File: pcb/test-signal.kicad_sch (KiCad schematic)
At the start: 9 parts, among them J3 Conn_Coaxial, U13 SN74LVC1G3157DCKR, U150 MCP4821

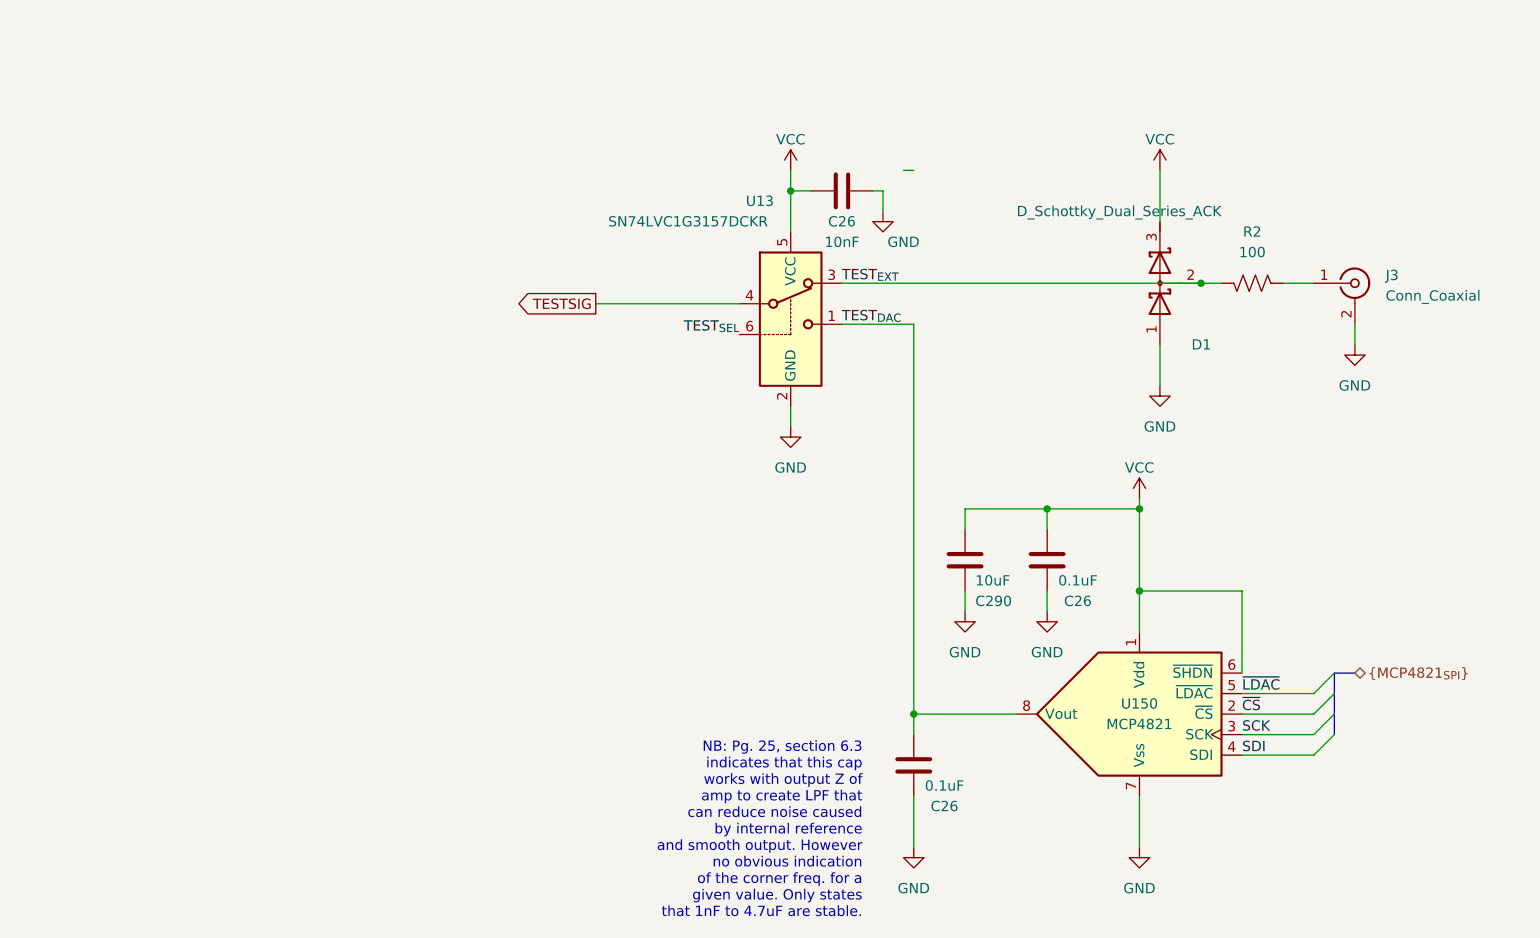
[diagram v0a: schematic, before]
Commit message: Remove battery power option
- This device needs user IO
- Battery power means there would need to be a touch screen or wireless
  connection. Too complex.
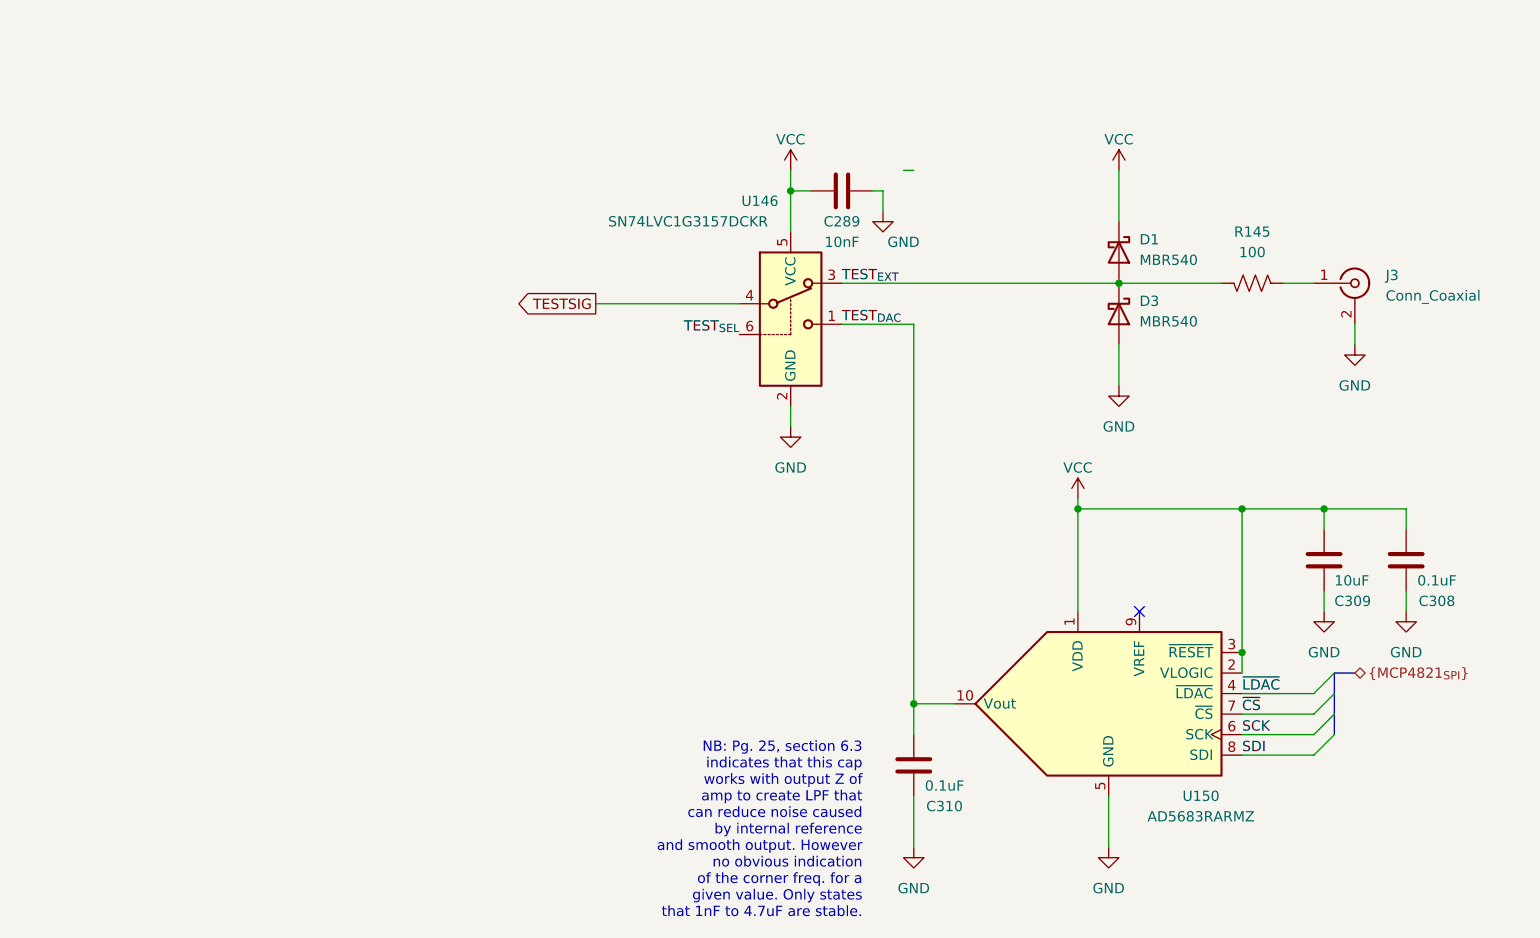
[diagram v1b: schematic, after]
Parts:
- removed D1: D_Schottky_Dual_Series_ACK, symbol Device:D_Schottky_Dual_Series_ACK
- removed U150: MCP4821, symbol Analog_DAC:MCP4821
- added D1, D3: MBR540, Diode_SMD:D_SOD-123, symbol Device:D_Schottky
- added U150: AD5683RARMZ, Package_SO:MSOP-10_3x3mm_P0.5mm, symbol open-ephys:AD568xR
- R145: renamed from R2; footprint Resistor_SMD:R_0805_2012Metric -> Resistor_SMD:R_0402_1005Metric
- renumbered C26 to C289, C26 to C308, C290 to C309, C26 to C310, U13 to U146
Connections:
- net GND: now also D3.2 (A), U150.5 (GND)
- net SCK: now also U150.6 (SCK)
- net SDI: now also U150.8 (SDI)
- net TEST_{DAC}: now also U150.10 (Vout)
- net TEST_{EXT}: now also D1.2 (A), D3.1 (K)
- net VCC: now also D1.1 (K), U150.1 (VDD), U150.2 (VLOGIC), U150.3 (~{RESET})
- net ~{CS}: now also U150.7 (~{CS})
- net ~{LDAC}: now also U150.4 (~{LDAC})
- no-connect marks 0 -> 1
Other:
- moved on the sheet: C308, C309

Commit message: Finished schematic, started routing
- There is a 8-channel motif that will need to be copied 16x on the
  board. I'm not sure the most efficient way to do this.
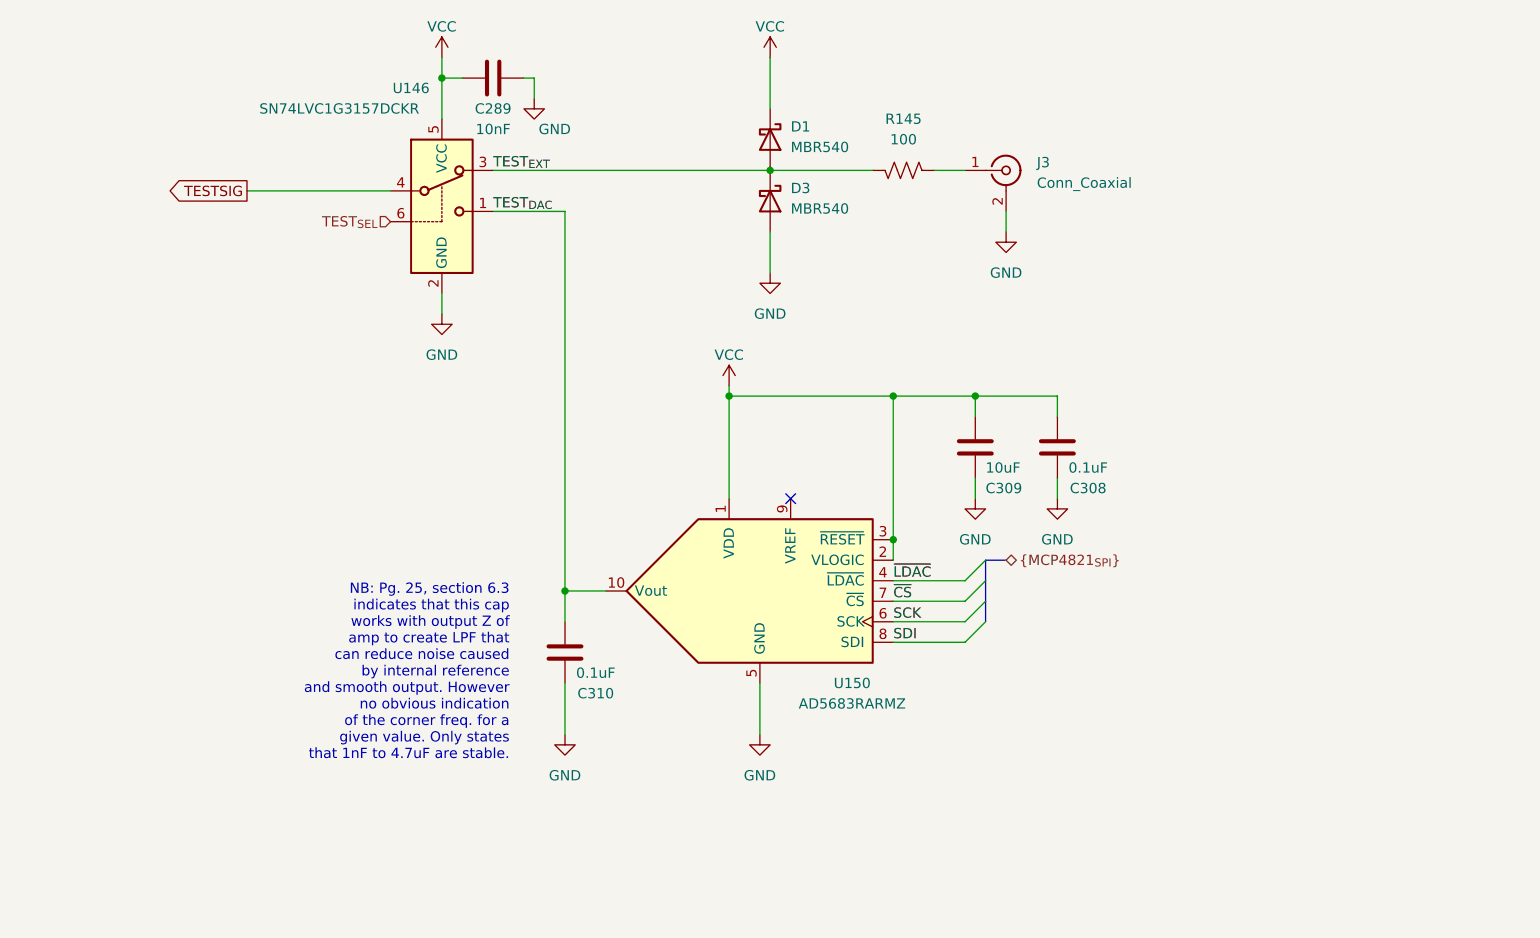
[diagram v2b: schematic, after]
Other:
- moved on the sheet: C289, C308, C309, C310, D1, D3, J3, R145, U146, U150

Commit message: Motif is repeated
- some components are grouped by function
- components are roughly organized within groups
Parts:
- renumbered C289 to C288, C310 to C289, C309 to C290, C308 to C291, D3 to D2, J3 to J5, R145 to R262, U146 to U147, U150 to U148
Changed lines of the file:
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@@
 		(dnp no)
 		(fields_autoplaced yes)
-		(property "Reference" "#PWR0604"
+		(property "Reference" "#PWR0723"
 			(at 127 132.08 0)
 			(effects
@@
 			(project "ephys-test-board"
 				(path "/ffaa6ffd-73fa-4da3-9ff1-78fa7369281f/a1b553e6-360f-440c-99f8-5680e9dd5803"
-					(reference "#PWR0604")
+					(reference "#PWR0723")
 					(unit 1)
 				)
@@
 		(on_board yes)
 		(dnp no)
-		(property "Reference" "C308"
+		(property "Reference" "C291"
 			(at 191.77 95.25 0)
 			(effects
@@
 			(project "ephys-test-board"
 				(path "/ffaa6ffd-73fa-4da3-9ff1-78fa7369281f/a1b553e6-360f-440c-99f8-5680e9dd5803"
-					(reference "C308")
+					(reference "C291")
 					(unit 1)
 				)
@@
 		(on_board yes)
 		(dnp no)
-		(property "Reference" "R145"
+		(property "Reference" "R262"
 			(at 168.91 49.53 90)
 			(effects
@@
 			(project "ephys-test-board"
 				(path "/ffaa6ffd-73fa-4da3-9ff1-78fa7369281f/a1b553e6-360f-440c-99f8-5680e9dd5803"
-					(reference "R145")
+					(reference "R262")
 					(unit 1)
 				)
@@
 		(dnp no)
 		(fields_autoplaced yes)
-		(property "Reference" "#PWR0566"
+		(property "Reference" "#PWR0729"
 			(at 181.61 69.85 0)
 			(effects
@@
 			(project "ephys-test-board"
 				(path "/ffaa6ffd-73fa-4da3-9ff1-78fa7369281f/a1b553e6-360f-440c-99f8-5680e9dd5803"
-					(reference "#PWR0566")
+					(reference "#PWR0729")
 					(unit 1)
 				)
@@
 		(on_board yes)
 		(dnp no)
-		(property "Reference" "#PWR0564"
+		(property "Reference" "#PWR0726"
 			(at 152.4 45.72 0)
 			(effects
@@
 			(project "ephys-test-board"
 				(path "/ffaa6ffd-73fa-4da3-9ff1-78fa7369281f/a1b553e6-360f-440c-99f8-5680e9dd5803"
-					(reference "#PWR0564")
+					(reference "#PWR0726")
 					(unit 1)
 				)
@@
 		(on_board yes)
 		(dnp no)
-		(property "Reference" "U150"
+		(property "Reference" "U148"
 			(at 162.56 119.38 0)
 			(effects
@@
 			(project "ephys-test-board"
 				(path "/ffaa6ffd-73fa-4da3-9ff1-78fa7369281f/a1b553e6-360f-440c-99f8-5680e9dd5803"
-					(reference "U150")
+					(reference "U148")
 					(unit 1)
 				)
@@
 		(on_board yes)
 		(dnp no)
-		(property "Reference" "#PWR0603"
+		(property "Reference" "#PWR0728"
 			(at 177.8 102.87 0)
 			(effects
@@
 			(project "ephys-test-board"
 				(path "/ffaa6ffd-73fa-4da3-9ff1-78fa7369281f/a1b553e6-360f-440c-99f8-5680e9dd5803"
-					(reference "#PWR0603")
+					(reference "#PWR0728")
 					(unit 1)
 				)
@@
 		(on_board yes)
 		(dnp no)
-		(property "Reference" "C289"
+		(property "Reference" "C288"
 			(at 118.11 48.26 90)
 			(effects
@@
 			(project "ephys-test-board"
 				(path "/ffaa6ffd-73fa-4da3-9ff1-78fa7369281f/a1b553e6-360f-440c-99f8-5680e9dd5803"
-					(reference "C289")
+					(reference "C288")
 					(unit 1)
 				)
@@
 		(on_board yes)
 		(dnp no)
-		(property "Reference" "#PWR0601"
+		(property "Reference" "#PWR0730"
 			(at 187.96 102.87 0)
 			(effects
@@
 			(project "ephys-test-board"
 				(path "/ffaa6ffd-73fa-4da3-9ff1-78fa7369281f/a1b553e6-360f-440c-99f8-5680e9dd5803"
-					(reference "#PWR0601")
+					(reference "#PWR0730")
 					(unit 1)
 				)
@@
 		(dnp no)
 		(fields_autoplaced yes)
-		(property "Reference" "J3"
+		(property "Reference" "J5"
 			(at 185.42 54.9032 0)
 			(effects
@@
 			(project "ephys-test-board"
 				(path "/ffaa6ffd-73fa-4da3-9ff1-78fa7369281f/a1b553e6-360f-440c-99f8-5680e9dd5803"
-					(reference "J3")
+					(reference "J5")
 					(unit 1)
 				)
@@
 		(on_board yes)
 		(dnp no)
-		(property "Reference" "#PWR0565"
+		(property "Reference" "#PWR0727"
 			(at 152.4 74.93 0)
 			(effects
@@
 			(project "ephys-test-board"
 				(path "/ffaa6ffd-73fa-4da3-9ff1-78fa7369281f/a1b553e6-360f-440c-99f8-5680e9dd5803"
-					(reference "#PWR0565")
+					(reference "#PWR0727")
 					(unit 1)
 				)
@@
 		(on_board yes)
 		(dnp no)
-		(property "Reference" "C309"
+		(property "Reference" "C290"
 			(at 179.07 95.25 0)
 			(effects
@@
 			(project "ephys-test-board"
 				(path "/ffaa6ffd-73fa-4da3-9ff1-78fa7369281f/a1b553e6-360f-440c-99f8-5680e9dd5803"
-					(reference "C309")
+					(reference "C290")
 					(unit 1)
 				)
@@
 		(on_board yes)
 		(dnp no)
-		(property "Reference" "#PWR0561"
+		(property "Reference" "#PWR0720"
 			(at 111.76 45.72 0)
 			(effects
@@
 			(project "ephys-test-board"
 				(path "/ffaa6ffd-73fa-4da3-9ff1-78fa7369281f/a1b553e6-360f-440c-99f8-5680e9dd5803"
-					(reference "#PWR0561")
+					(reference "#PWR0720")
 					(unit 1)
 				)
@@
 		(on_board yes)
 		(dnp no)
-		(property "Reference" "#PWR0563"
+		(property "Reference" "#PWR0722"
 			(at 123.19 53.34 0)
 			(effects
@@
 			(project "ephys-test-board"
 				(path "/ffaa6ffd-73fa-4da3-9ff1-78fa7369281f/a1b553e6-360f-440c-99f8-5680e9dd5803"
-					(reference "#PWR0563")
+					(reference "#PWR0722")
 					(unit 1)
 				)
@@
 		(on_board yes)
 		(dnp no)
-		(property "Reference" "U146"
+		(property "Reference" "U147"
 			(at 107.95 45.72 0)
 			(effects
@@
 			(project "ephys-test-board"
 				(path "/ffaa6ffd-73fa-4da3-9ff1-78fa7369281f/a1b553e6-360f-440c-99f8-5680e9dd5803"
-					(reference "U146")
+					(reference "U147")
 					(unit 1)
 				)
@@
 		(dnp no)
 		(fields_autoplaced yes)
-		(property "Reference" "#PWR0562"
+		(property "Reference" "#PWR0721"
 			(at 111.76 80.01 0)
 			(effects
@@
 			(project "ephys-test-board"
 				(path "/ffaa6ffd-73fa-4da3-9ff1-78fa7369281f/a1b553e6-360f-440c-99f8-5680e9dd5803"
-					(reference "#PWR0562")
+					(reference "#PWR0721")
 					(unit 1)
 				)
@@
 		(dnp no)
 		(fields_autoplaced yes)
-		(property "Reference" "#PWR0602"
+		(property "Reference" "#PWR0725"
 			(at 151.13 132.08 0)
 			(effects
@@
 			(project "ephys-test-board"
 				(path "/ffaa6ffd-73fa-4da3-9ff1-78fa7369281f/a1b553e6-360f-440c-99f8-5680e9dd5803"
-					(reference "#PWR0602")
+					(reference "#PWR0725")
 					(unit 1)
 				)
@@
 		(dnp no)
 		(fields_autoplaced yes)
-		(property "Reference" "D3"
+		(property "Reference" "D2"
 			(at 154.94 58.1025 90)
 			(effects
@@
 			(project "ephys-test-board"
 				(path "/ffaa6ffd-73fa-4da3-9ff1-78fa7369281f/a1b553e6-360f-440c-99f8-5680e9dd5803"
-					(reference "D3")
+					(reference "D2")
 					(unit 1)
 				)
@@
 		(on_board yes)
 		(dnp no)
-		(property "Reference" "#PWR0600"
+		(property "Reference" "#PWR0724"
 			(at 147.32 86.36 0)
 			(effects
@@
 			(project "ephys-test-board"
 				(path "/ffaa6ffd-73fa-4da3-9ff1-78fa7369281f/a1b553e6-360f-440c-99f8-5680e9dd5803"
-					(reference "#PWR0600")
+					(reference "#PWR0724")
 					(unit 1)
 				)
@@
 		(on_board yes)
 		(dnp no)
-		(property "Reference" "C310"
+		(property "Reference" "C289"
 			(at 130.81 120.65 0)
 			(effects
@@
 			(project "ephys-test-board"
 				(path "/ffaa6ffd-73fa-4da3-9ff1-78fa7369281f/a1b553e6-360f-440c-99f8-5680e9dd5803"
-					(reference "C310")
-					(unit 1)
-				)
+					(reference "C289")
+					(unit 1)
+				)

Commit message: Initial Rev. A schematic
- I think this has everything we need for revision A
- Battery charge indication via the OLED display
- User interface via rotary encoder/select switch
- Cycle through affected individual channels, none, or all
- Cycle through amplitudes
- Cycle through frequencies
- Select signal source
- Cycle through pre-loaded channel maps?
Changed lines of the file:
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@@
 	)
 	(hierarchical_label "{MCP4821_{SPI}}"
-		(shape bidirectional)
+		(shape input)
 		(at 181.61 104.14 0)
 		(fields_autoplaced yes)

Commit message: More schematic improvements
- Add pullups to i2c bus
- Add test points
- Ready for initial routing
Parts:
- added TP13: VCC, TestPoint:TestPoint_Pad_D2.0mm, symbol Connector:TestPoint
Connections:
- net TESTSIG: now also TP13.1
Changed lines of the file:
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@@
+	)
+	(junction
+		(at 80.01 58.42)
+		(diameter 0)
+		(color 0 0 0 0)
 	)
 	(junction
@@
 	(wire
 		(pts
+			(xy 80.01 55.88) (xy 80.01 58.42)
+		)
+		(stroke
+			(width 0)
+			(type default)
+		)
+	)
+	(wire
+		(pts
 			(xy 111.76 44.45) (xy 111.76 49.53)
 		)
@@
 	(wire
 		(pts
-			(xy 87.63 58.42) (xy 105.41 58.42)
+			(xy 71.12 58.42) (xy 80.01 58.42)
 		)
 		(stroke
@@
 		(pts
 			(xy 187.96 83.82) (xy 187.96 86.36)
+		)
+		(stroke
+			(width 0)
+			(type default)
+		)
+	)
+	(wire
+		(pts
+			(xy 80.01 58.42) (xy 105.41 58.42)
 		)
 		(stroke
@@
 	(global_label "TESTSIG"
 		(shape output)
-		(at 87.63 58.42 180)
+		(at 71.12 58.42 180)
 		(fields_autoplaced yes)
 		(effects
@@
 		)
 		(property "Intersheetrefs" "${INTERSHEET_REFS}"
-			(at 77.2668 58.42 0)
+			(at 60.7568 58.42 0)
 			(effects
 				(font
@@
 					(unit 1)
 				)
+			)
+		)
+	)
+	(symbol
+		(lib_id "Connector:TestPoint")
+		(at 80.01 55.88 0)
+		(unit 1)
+		(exclude_from_sim no)
+		(in_bom yes)
+		(on_board yes)
+		(dnp no)
+		(property "Reference" "TP13"
+			(at 80.772 51.308 0)
+			(effects
+				(font
+					(size 1.27 1.27)
+				)
+				(justify left)
+			)
+		)
+		(property "Value" "VCC"
+			(at 80.772 53.848 0)
+			(effects
+				(font
+					(size 1.27 1.27)
+				)
+				(justify left)
+				(hide yes)
+			)
+		)
+		(property "Footprint" "TestPoint:TestPoint_Pad_D2.0mm"
+			(at 85.09 55.88 0)
+			(effects
+				(font
+					(size 1.27 1.27)
+				)
+				(hide yes)
+			)
+		)
+		(property "Datasheet" "~"
+			(at 85.09 55.88 0)
+			(effects
+				(font
+					(size 1.27 1.27)
+				)
+				(hide yes)
+			)
+		)
+		(property "Description" "test point"
+			(at 80.01 55.88 0)
+			(effects
+				(font
+					(size 1.27 1.27)
+				)
+				(hide yes)
+			)
+		)
+		(pin "1"
+		)
+		(instances
+			(project "ephys-test-board"
+				(path "/ffaa6ffd-73fa-4da3-9ff1-78fa7369281f/a1b553e6-360f-440c-99f8-5680e9dd5803"
+					(reference "TP13")
+					(unit 1)
+				)

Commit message: Start routing rev. A
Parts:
- J5: value Conn_Coaxial -> 731000105; footprint Connector_Coaxial:BNC_Amphenol_B6252HB-NPP3G-50_Horizontal -> open-ephys:BNC_MOLEX_0731000105
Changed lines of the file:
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@@
 			)
 		)
-		(property "Value" "Conn_Coaxial"
+		(property "Value" "731000105"
 			(at 185.42 57.4432 0)
 			(effects
@@
 			)
 		)
-		(property "Footprint" "Connector_Coaxial:BNC_Amphenol_B6252HB-NPP3G-50_Horizontal"
+		(property "Footprint" "open-ephys:BNC_MOLEX_0731000105"
 			(at 181.61 55.88 0)
 			(effects
@@
 			)
 		)
-		(property "Datasheet" "~"
+		(property "Datasheet" "https://www.molex.com/content/dam/molex/molex-dot-com/products/automated/en-us/salesdrawingpdf/731/73100/731000105_sd.pdf?inline"
 			(at 181.61 55.88 0)
 			(effects
